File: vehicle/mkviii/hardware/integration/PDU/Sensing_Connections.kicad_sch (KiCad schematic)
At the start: 3 parts, among them J1 pcie_x1_connector, J3 pcie_x1_connector, J4 pcie_x1_connector

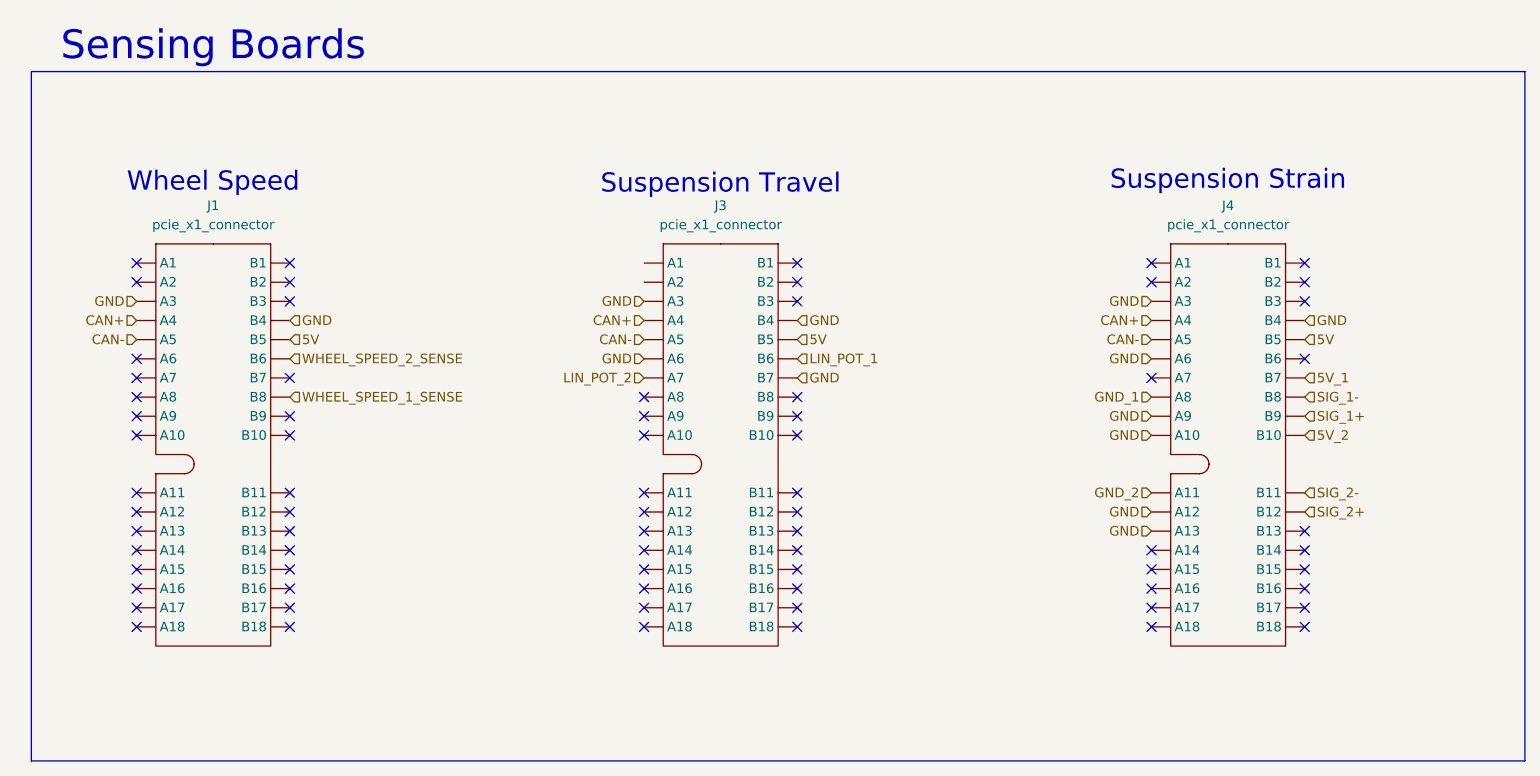
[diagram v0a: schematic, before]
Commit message: Start work on fixing broken footprints
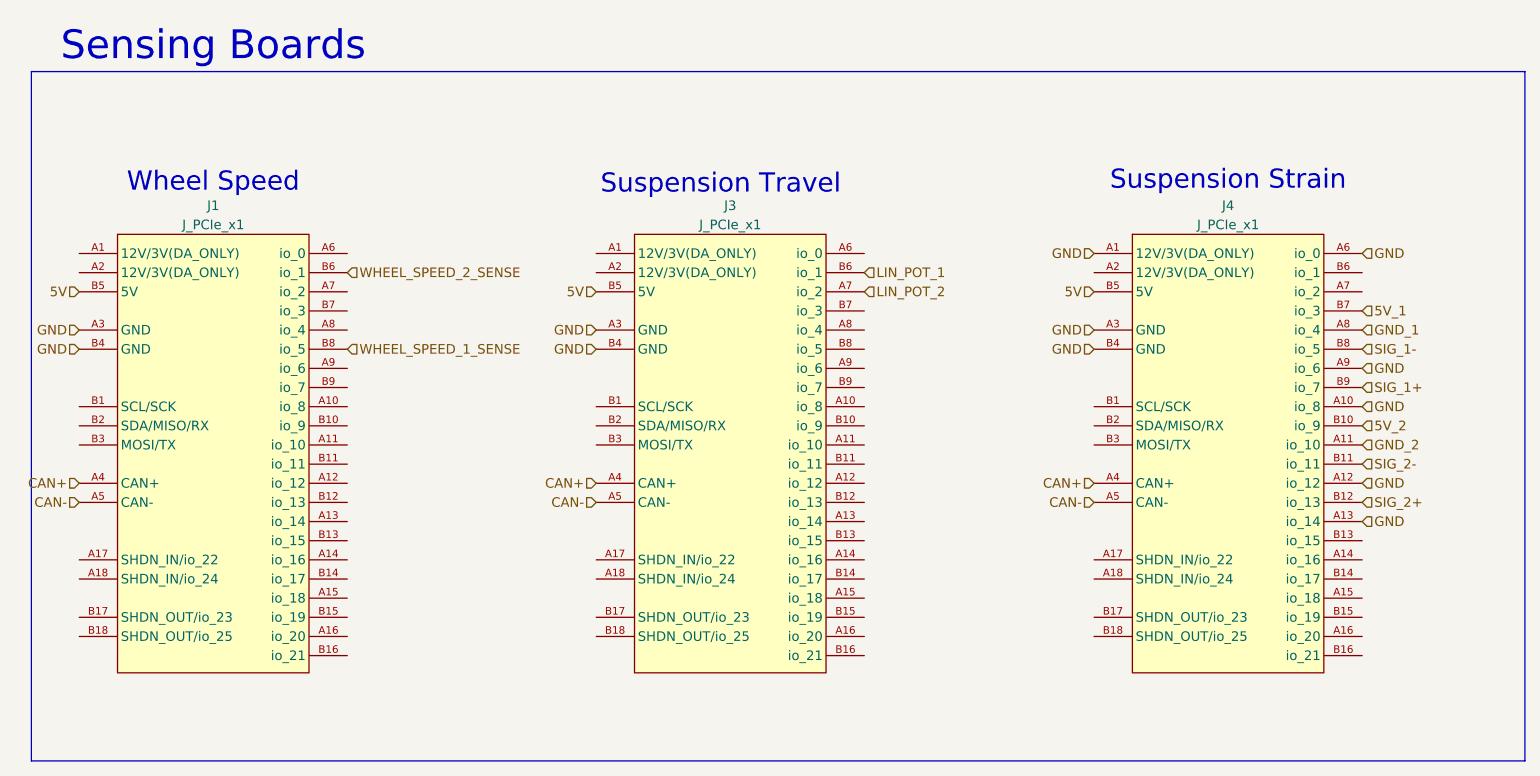
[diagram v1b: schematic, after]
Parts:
- removed J1, J3, J4: pcie_x1_connector, OEM:J_PCIe_x1, symbol oem:pcie_x1_connector
- added J1, J3, J4: J_PCIe_x1, OEM:te_pcie_x1_connector, symbol OEM:J_PCIe_x1
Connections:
- net 5V: now also J1.B5 (5V), J3.B5 (5V), J4.B5 (5V)
- net 5V_1: now also J4.B7 (io_3)
- net 5V_2: now also J4.B10 (io_9)
- net CAN+: now also J1.A4 (CAN+), J3.A4 (CAN+), J4.A4 (CAN+)
- net CAN-: now also J1.A5 (CAN-), J3.A5 (CAN-), J4.A5 (CAN-)
- net GND: now also J1.A3 (GND), J1.B4 (GND), J3.A3 (GND), J3.B4 (GND), J4.A1 (12V/3V(DA_ONLY)), J4.A10 (io_8), J4.A12 (io_12), J4.A13 (io_14), J4.A3 (GND), J4.A6 (io_0), J4.A9 (io_6), J4.B4 (GND)
- net GND_1: now also J4.A8 (io_4)
- net GND_2: now also J4.A11 (io_10)
- net LIN_POT_1: now also J3.B6 (io_1)
- net LIN_POT_2: now also J3.A7 (io_2)
- net SIG_1+: now also J4.B9 (io_7)
- net SIG_1-: now also J4.B8 (io_5)
- net SIG_2+: now also J4.B12 (io_13)
- net SIG_2-: now also J4.B11 (io_11)
- net WHEEL_SPEED_1_SENSE: now also J1.B8 (io_5)
- net WHEEL_SPEED_2_SENSE: now also J1.B6 (io_1)
- no-connect marks 72 -> 0

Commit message: Start work on PCB (The parts are placed)
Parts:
- J1, J3, J4: footprint OEM:te_pcie_x1_connector -> OEM:J_PCIe_x1
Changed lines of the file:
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@@
 			)
 		)
-		(property "Footprint" "OEM:te_pcie_x1_connector"
+		(property "Footprint" "OEM:J_PCIe_x1"
 			(at 140.97 62.23 0)
 			(hide yes)
@@
 			)
 		)
-		(property "Footprint" "OEM:te_pcie_x1_connector"
+		(property "Footprint" "OEM:J_PCIe_x1"
 			(at 72.39 62.23 0)
 			(hide yes)
@@
 			)
 		)
-		(property "Footprint" "OEM:te_pcie_x1_connector"
+		(property "Footprint" "OEM:J_PCIe_x1"
 			(at 207.01 62.23 0)
 			(hide yes)
